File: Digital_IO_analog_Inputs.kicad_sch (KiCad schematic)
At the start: 40 parts, among them J3 302-S101, J5 OSTTC020162, J7 OSTTC030162, J9 0022232031, Q3 BC817-25LT1G, Q4 BC817-25LT1G, U17 ISO1211DR, U24 ISO1211DR, U26 ISO1211DR

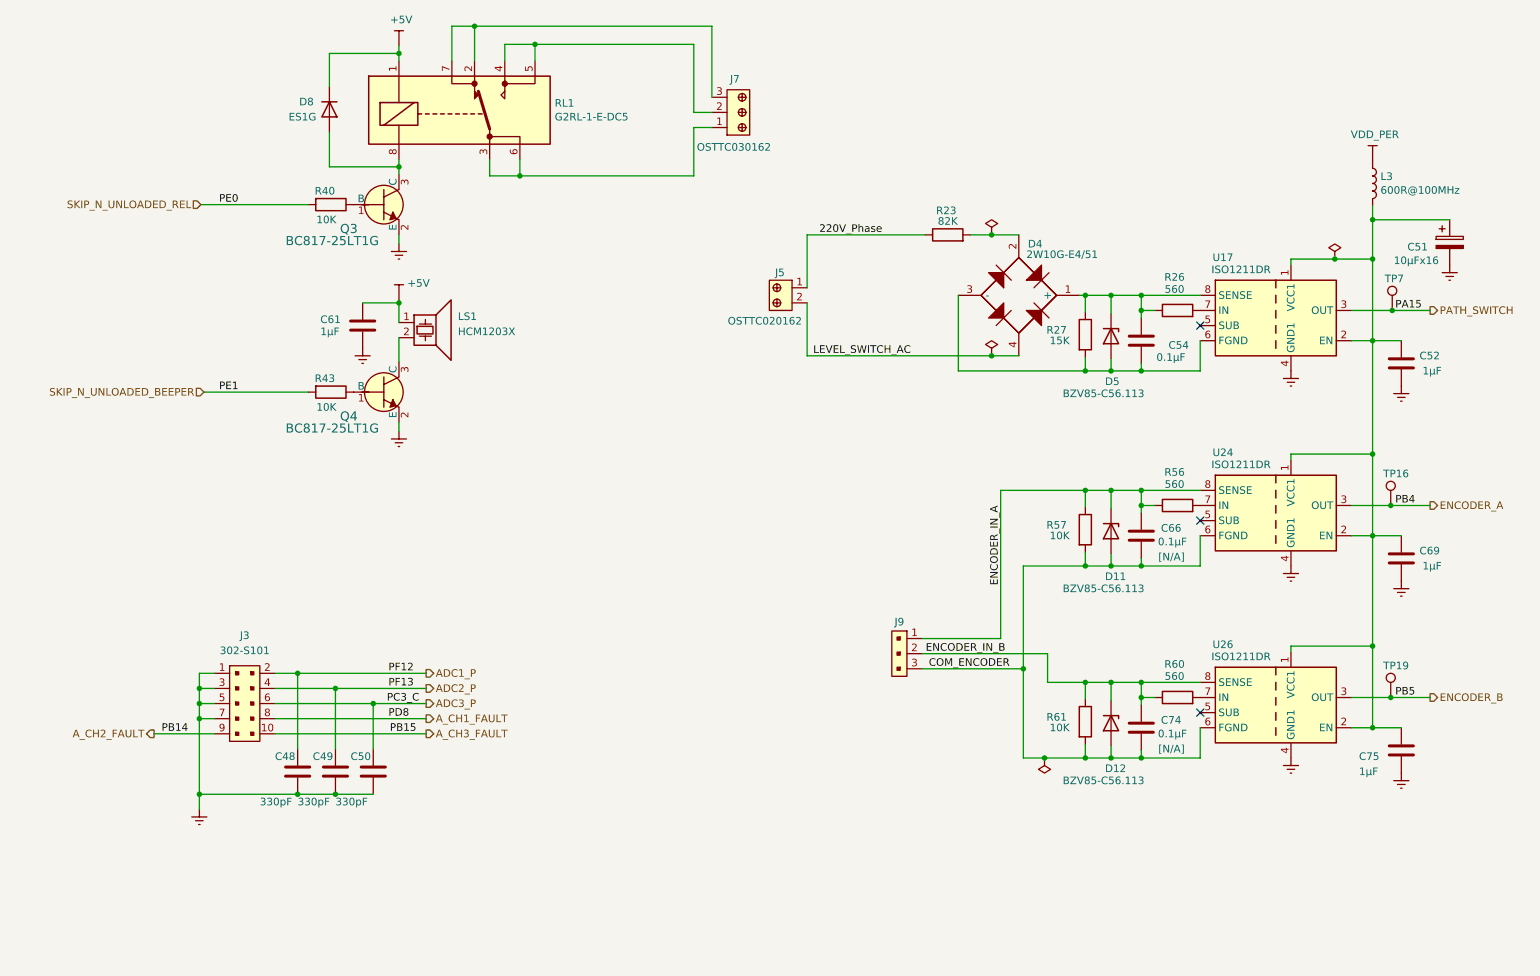
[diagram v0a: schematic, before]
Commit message: KiCAD6.0 scheema rules check done
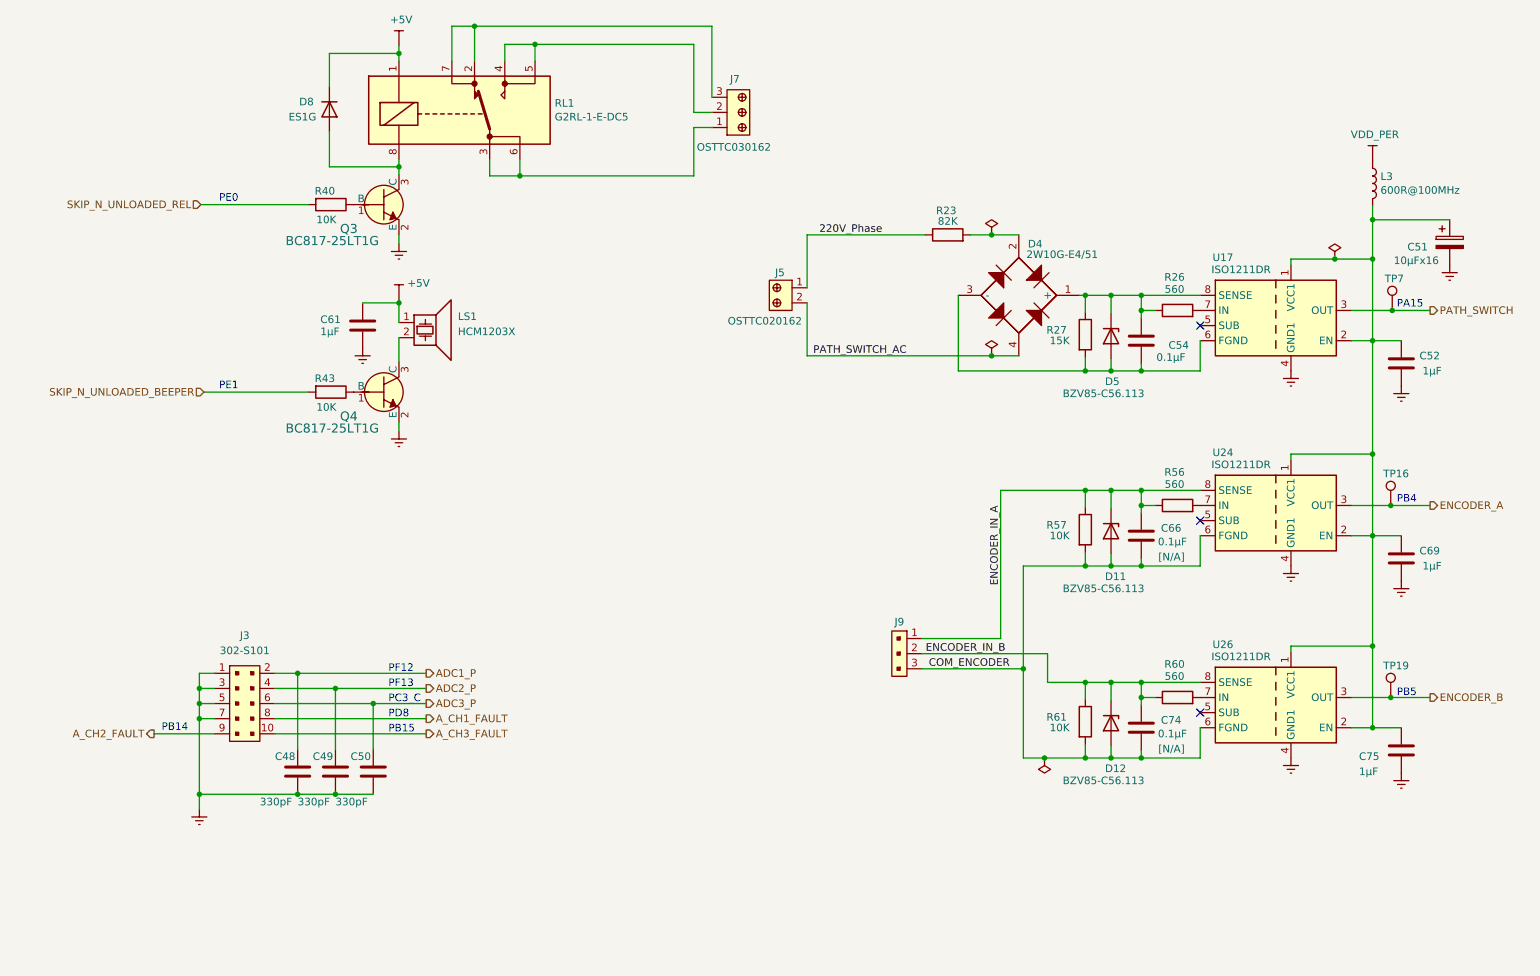
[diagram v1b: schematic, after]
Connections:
- net LEVEL_SWITCH_AC renamed PATH_SWITCH_AC
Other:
- note added: "PA15"
- note added: "PB14"
- note added: "PB15"
- note added: "PB4"
- note added: "PB5"
- note added: "PC3_C"
- note added: "PD8"
- note added: "PE0"
- note added: "PE1"
- note added: "PF12"
- note added: "PF13"
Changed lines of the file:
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@@
     (stroke (width 0) (type default) (color 0 0 0 0))
+  )
+  (text "PE1" (at 50.292 90.932 0)
+    (effects (font (size 1.27 1.27)) (justify left bottom))
+  )
+  (text "PD8" (at 78.74 146.05 0)
+    (effects (font (size 1.27 1.27)) (justify left bottom))
+  )
+  (text "PF13" (at 78.74 140.97 0)
+    (effects (font (size 1.27 1.27)) (justify left bottom))
+  )
+  (text "PF12" (at 78.74 138.43 0)
+    (effects (font (size 1.27 1.27)) (justify left bottom))
+  )
+  (text "PA15" (at 248.158 77.216 0)
+    (effects (font (size 1.27 1.27)) (justify left bottom))
+  )
+  (text "PB15" (at 78.74 148.59 0)
+    (effects (font (size 1.27 1.27)) (justify left bottom))
+  )
+  (text "PB14" (at 40.64 148.336 0)
+    (effects (font (size 1.27 1.27)) (justify left bottom))
+  )
+  (text "PE0" (at 50.292 59.436 0)
+    (effects (font (size 1.27 1.27)) (justify left bottom))
+  )
+  (text "PB5" (at 248.158 142.494 0)
+    (effects (font (size 1.27 1.27)) (justify left bottom))
+  )
+  (text "PB4" (at 248.158 109.982 0)
+    (effects (font (size 1.27 1.27)) (justify left bottom))
+  )
+  (text "PC3_C" (at 78.74 143.51 0)
+    (effects (font (size 1.27 1.27)) (justify left bottom))
   )
   (label "ENCODER_IN_B" (at 169.0116 135.128 0)
@@
     (effects (font (size 1.27 1.27)) (justify right bottom))
   )
-  (label "PD8" (at 78.74 146.05 0)
-    (effects (font (size 1.27 1.27)) (justify left bottom))
-  )
-  (label "PC3_C" (at 78.486 143.51 0)
-    (effects (font (size 1.27 1.27)) (justify left bottom))
-  )
-  (label "PF12" (at 78.74 138.43 0)
-    (effects (font (size 1.27 1.27)) (justify left bottom))
-  )
-  (label "PE1" (at 50.292 91.186 0)
-    (effects (font (size 1.27 1.27)) (justify left bottom))
-  )
-  (label "LEVEL_SWITCH_AC" (at 150.114 85.09 0)
-    (effects (font (size 1.27 1.27)) (justify left bottom))
-  )
-  (label "PE0" (at 50.292 59.69 0)
+  (label "PATH_SWITCH_AC" (at 150.114 85.09 0)
     (effects (font (size 1.27 1.27)) (justify left bottom))
   )
@@
     (effects (font (size 1.27 1.27)) (justify right bottom))
   )
-  (label "PB14" (at 40.64 148.59 0)
-    (effects (font (size 1.27 1.27)) (justify left bottom))
-  )
-  (label "PB15" (at 78.994 148.59 0)
-    (effects (font (size 1.27 1.27)) (justify left bottom))
-  )
-  (label "PB5" (at 247.904 142.494 0)
-    (effects (font (size 1.27 1.27)) (justify left bottom))
-  )
-  (label "PB4" (at 247.904 110.236 0)
-    (effects (font (size 1.27 1.27)) (justify left bottom))
-  )
   (label "220V_Phase" (at 151.13 64.77 0)
     (effects (font (size 1.27 1.27)) (justify left bottom))
   )
-  (label "PA15" (at 247.904 77.47 0)
-    (effects (font (size 1.27 1.27)) (justify left bottom))
-  )
-  (label "PF13" (at 78.74 140.97 0)
-    (effects (font (size 1.27 1.27)) (justify left bottom))
-  )

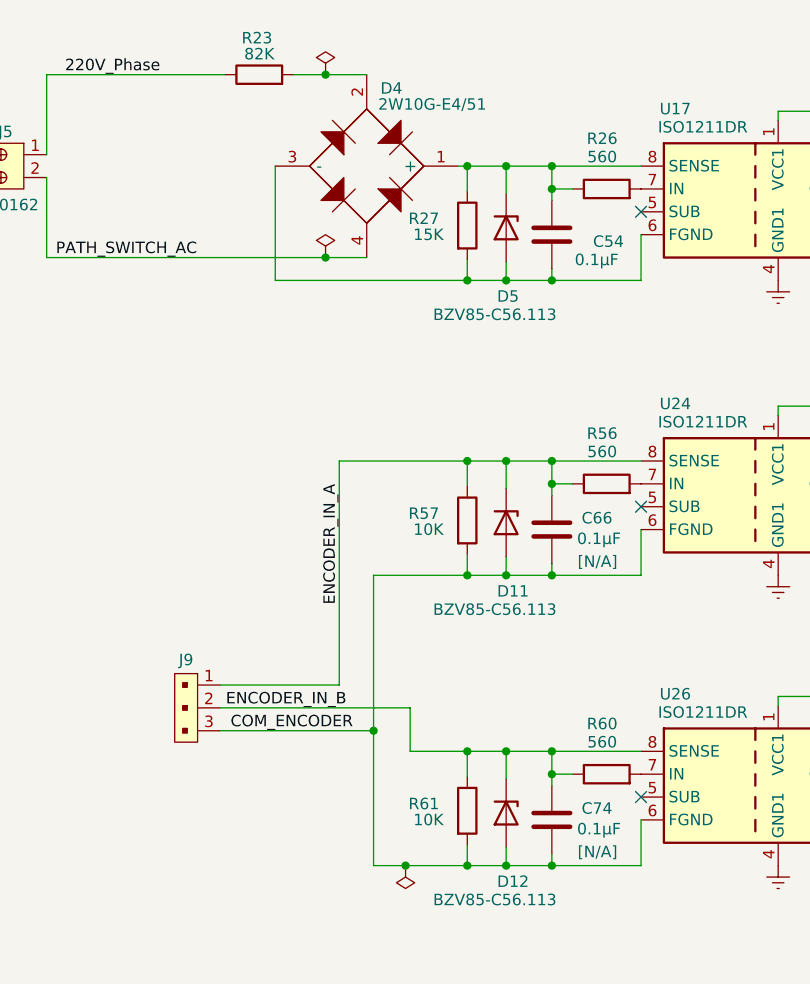
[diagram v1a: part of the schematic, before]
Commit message: digital inputs refactoring
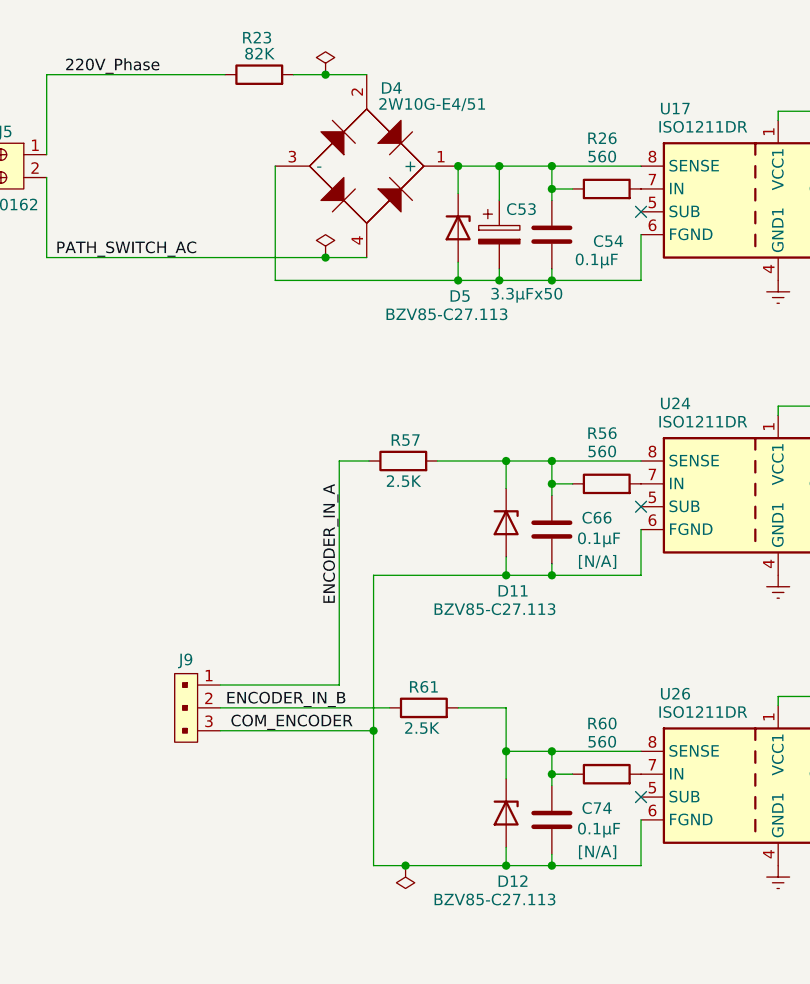
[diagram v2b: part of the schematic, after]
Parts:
- removed R27: 15K, Resistor_THT:R_Axial_DIN0207_L6.3mm_D2.5mm_P10.16mm_Horizontal, symbol Device:R
- added C53: 3.3µFx50, Capacitor_Tantalum_SMD:CP_EIA-6032-15_Kemet-U, symbol Device:CP
- D11, D12, D5: value BZV85-C56.113 -> BZV85-C27.113
- R57, R61: value 10K -> 2.5K
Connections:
- net COM_ENCODER: no longer R57.2, R61.2
- net ENCODER_IN_A: no longer C66.1, D11.1 (K), R56.1, U24.8 (SENSE)
- net ENCODER_IN_B: no longer C74.1, D12.1 (K), R60.1, U26.8 (SENSE)
- net at C54.1, D4.1 (+), D5.1 (K)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: now also C53.1
- net at C54.2, D4.3 (-), D5.2 (A)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: now also C53.2
- new net: C66.1, D11.1 (K), R56.1, R57.2, U24.8 (SENSE)
- new net: C74.1, D12.1 (K), R60.1, R61.2, U26.8 (SENSE)
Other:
- moved on the sheet: D5, R57, R61

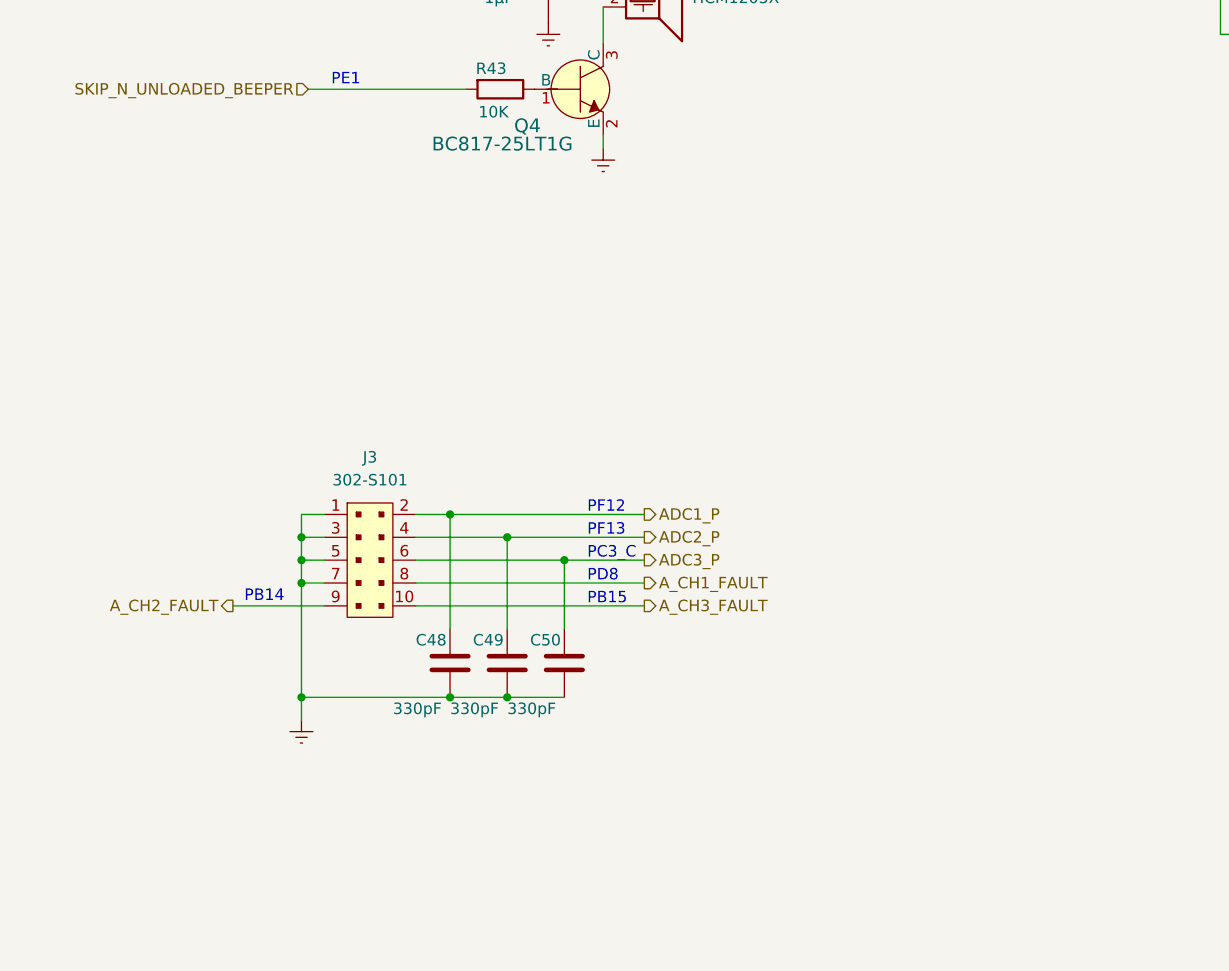
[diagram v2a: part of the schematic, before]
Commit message: Indication LEDs added
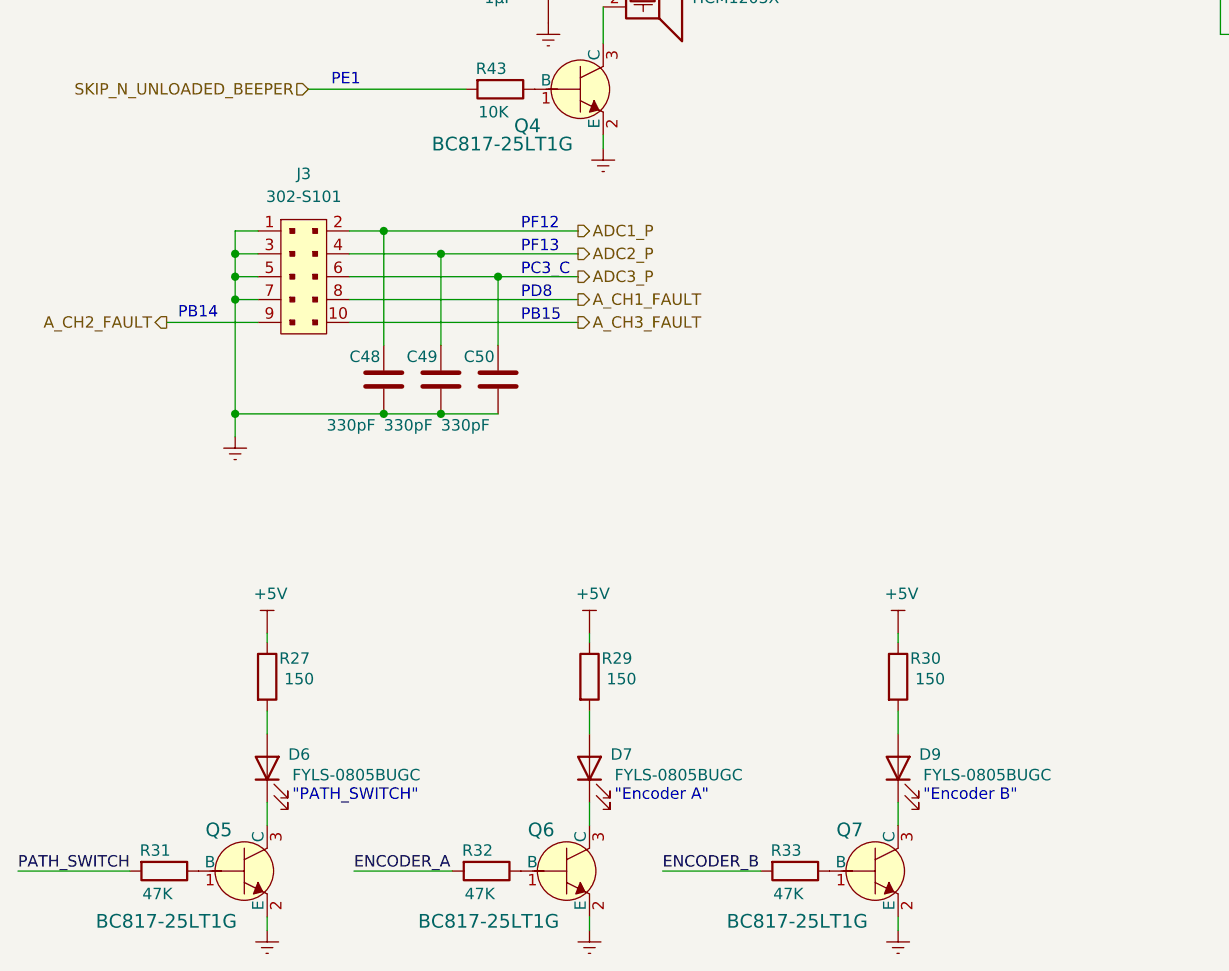
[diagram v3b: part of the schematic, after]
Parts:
- added D6, D7, D9: FYLS-0805BUGC, LED_SMD:LED_0805_2012Metric, symbol Device:LED
- added Q5, Q6, Q7: BC817-25LT1G, digikey-footprints:SOT-23-3, symbol dk_Transistors-Bipolar-BJT-Single:BC817-25LT1G
- added R27, R29, R30: 150, Resistor_SMD:R_0805_2012Metric_Pad1.20x1.40mm_HandSolder, symbol Device:R
- added R31, R32, R33: 47K, Resistor_SMD:R_0805_2012Metric_Pad1.20x1.40mm_HandSolder, symbol Device:R
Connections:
- net +5V: now also R27.1, R29.1, R30.1
- net ENCODER_A: now also R32.2
- net ENCODER_B: now also R33.2
- net GNDREF: now also Q5.2 (E), Q6.2 (E), Q7.2 (E)
- net PATH_SWITCH: now also R31.2
- new net: Q7.1 (B), R33.1
- new net: D9.1 (K), Q7.3 (C)
- new net: D9.2 (A), R30.2
- new net: D6.2 (A), R27.2
- new net: D6.1 (K), Q5.3 (C)
- new net: D7.2 (A), R29.2
- new net: Q5.1 (B), R31.1
- new net: Q6.1 (B), R32.1
- new net: D7.1 (K), Q6.3 (C)
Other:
- note added: ""Encoder A""
- note added: ""Encoder B""
- note added: ""PATH_SWITCH""
- moved on the sheet: C48, C49, C50, J3
